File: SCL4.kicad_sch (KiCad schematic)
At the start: 4 parts

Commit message: ERC passes
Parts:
- added J1: Siemens_A1010-A263, symbol siemens_a1010-a263:Siemens_A1010-A263
- added J2: Conn_01x08, symbol Connector_Generic:Conn_01x08
- added J3: 5V out, symbol Connector:Screw_Terminal_01x02
- added J4: spare1, symbol Connector:Conn_01x01_Male
- added J5: SP1, symbol Connector:Conn_01x02_Male
- added J6: spare2, symbol Connector:Conn_01x01_Male
- added J7: SP2, symbol Connector:Conn_01x02_Male
- added JP1: LSA, symbol Jumper:Jumper_3_Open
- added JP2: LSB, symbol Jumper:Jumper_3_Open
- added JP3: LOCAL, symbol Jumper:Jumper_3_Open
- added JP4: NEXT, symbol Jumper:Jumper_3_Open
- added JP5: SYSTEM, symbol Jumper:Jumper_3_Open
- added R1, R2, R3, R4, R5, R6: 51R, symbol Device:R
- added R7, R8: 10K, symbol Device:R
- added U1: MC10H125 (20PLCC), symbol Interface:MC10H125 (20PLCC)
- added U2: MC10H124 (20PLCC), symbol Interface:MC10H124 (20PLCC)
- added U3: TRAM Size 2, symbol Transputer:TRAM Size 2
- added U5, U6: MC3487DX, Package_SO:SOIC-16_3.9x9.9mm_P1.27mm, symbol Interface_LineDriver:MC3487DX
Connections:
- net +48V: now also J1.P2 (48V+)
- net +5V: now also J3.2 (Pin_2), JP1.3 (B), JP2.3 (B), JP3.3 (B), JP4.3 (B), JP5.3 (B), U1.12 (Vcc), U2.12 (Vcc), U2.8 (CS), U3.19 (Vcc), U3.3 (Vcc), U5.12 (ENABLE), U5.12 (ENABLE), U5.16 (VCC), U5.16 (VCC), U5.16 (VCC), U5.16 (VCC), U5.4 (ENABLE), U5.4 (ENABLE), U6.12 (ENABLE), U6.12 (ENABLE), U6.16 (VCC), U6.16 (VCC), U6.16 (VCC), U6.16 (VCC), U6.4 (ENABLE), U6.4 (ENABLE)
- net -48V: now also J1.P3 (48V-)
- net -5V: now also U1.10 (Vee), U2.10 (Vee)
- net GND: now also J1.A54 (GND), J1.B1 (GND), J1.B2 (GND), J1.B3 (GND), J1.B6 (GND), J1.P1 (Gnd), J1.P4 (Stat_Gnd), J1.P5 (Gnd), J1.P6 (Gnd), J2.6 (Pin_6), J3.1 (Pin_1), JP1.1 (A), JP2.1 (A), JP3.1 (A), JP4.1 (A), JP5.1 (A), R3.2, R4.2, R5.2, R6.2, U1.20 (GND), U2.20 (GND), U3.14 (GND), U3.30 (GND), U5.8 (GND), U5.8 (GND), U5.8 (GND), U5.8 (GND), U6.8 (GND), U6.8 (GND), U6.8 (GND), U6.8 (GND)
- new net: JP1.2 (C), U3.6 (SpeedA)
- new net: JP4.2 (C), U5.9 (INPUT)
- new net: JP3.2 (C), U5.1 (INPUT)
- new net: JP2.2 (C), U3.7 (SpeedB)
- new net: J7.1 (Pin_1), U5.13 (OUT-)
- new net: J7.2 (Pin_2), U5.14 (OUT+)
- new net: R7.2, R8.2
- new net: JP5.2 (C), U6.15 (INPUT)
- new net: J6.1 (Pin_1), U5.15 (INPUT)
- new net: J5.1 (Pin_1), U5.5 (OUT-)
- new net: J5.2 (Pin_2), U5.6 (OUT+)
- new net: J4.1 (Pin_1), U5.7 (INPUT)
- new net ANALYSE: J1.A22 (/H2ANALYSE), J1.B22 (H1ANALYSE), U6.6 (OUT+)
- new net BYTE: J1.A25 (H2BYTE), J1.B25 (H1BYTE), U6.10 (OUT+)
- new net L2IN: J1.A1 (L2IN), R1.1, U1.14 (Cin)
- new net L2OUT: J1.A4 (L2OUT), R6.1, U2.19 (Cout)
- new net L3IN: J1.A7 (L3IN), R2.1, U1.19 (Din)
- new net L3OUT: J1.A10 (L3OUT), R4.1, U2.18 (Dout)
- new net LOCAL: J1.A27 (H2LOCAL), J1.B27 (H1LOCAL), U5.2 (OUT+)
- new net NEXT: J1.A31 (H2NEXT), J1.B31 (H1NEXT), U5.10 (OUT+)
- new net RESET: J1.A20 (/H2RESET), J1.B20 (H1RESET), U6.2 (OUT+)
- new net SYSTEM: J1.A23 (H2SYSTEM), J1.B23 (H1SYSYSTEM), U6.14 (OUT+)
- new net TAnalyse: J2.5 (Pin_5), U3.25 (Analyse), U6.7 (INPUT)
- new net TByte: J2.8 (Pin_8), U6.9 (INPUT)
- new net TClk: J2.1 (Pin_1), U3.8 (ClockIn)
- new net TL0In: J2.2 (Pin_2), U3.29 (L0in)
- new net TL0Out: J2.3 (Pin_3), U3.28 (L0out)
- new net TL2in: R8.1, U1.15 (Cout), U3.2 (L2in)
- new net TL2out: U2.13 (Cin), U3.1 (L2out)
- new net TL3in: R7.1, U1.17 (Dout), U3.32 (L3in)
- new net TL3out: U2.14 (Din), U3.31 (L3out)
- new net TNotError: J2.7 (Pin_7), U3.27 (/Error)
- new net TReset: J2.4 (Pin_4), U3.26 (Reset), U6.1 (INPUT)
- new net /ANALYSE: J1.A21 (H2ANALYSE), J1.B21 (/H1ANALYSE), U6.5 (OUT-)
- new net /BYTE: J1.A26 (/H2BYTE), J1.B26 (/H1BYTE), U6.11 (OUT-)
- new net /L2IN: J1.A2 (/L2IN), R1.2, U1.13 (/Cin)
- new net /L2OUT: J1.A5 (/L2OUT), R5.1, U2.15 (/Cout)
- new net /L3IN: J1.A8 (/L3IN), R2.2, U1.18 (/Din)
- new net /L3OUT: J1.A11 (/L3OUT), R3.1, U2.17 (/Dout)
- new net /LOCAL: J1.A28 (/H2LOCAL), J1.B28 (/H1LOCAL), U5.3 (OUT-)
- new net /NEXT: J1.A32 (/H2NEXT), J1.B32 (/H1NEXT), U5.11 (OUT-)
- new net /RESET: J1.A19 (H2RESET), J1.B19 (/H1RESET), U6.3 (OUT-)
- new net /SYSTEM: J1.A24 (/H2SYSTEM), J1.B24 (/H1SYSYSTEM), U6.13 (OUT-)
- no-connect marks 5 -> 239
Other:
- moved on the sheet: C1, C2, PS1, PS2

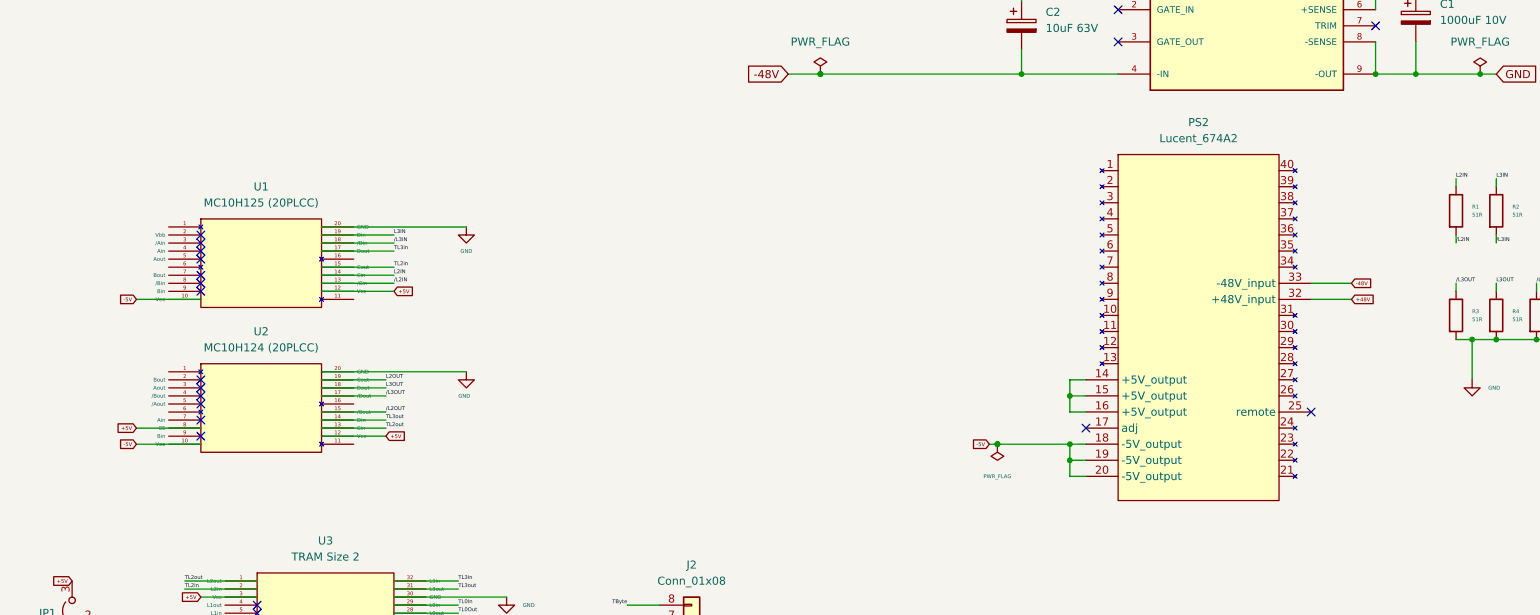
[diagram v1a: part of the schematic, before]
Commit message: swap abcd on siedecon
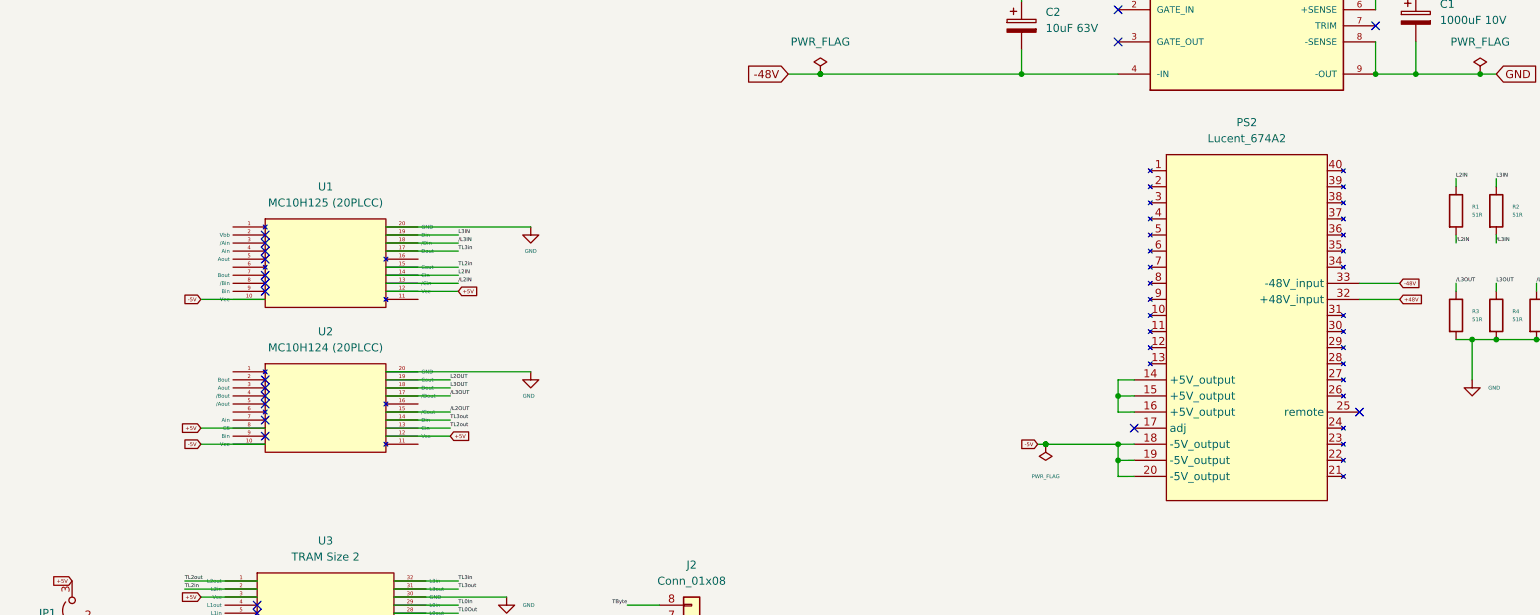
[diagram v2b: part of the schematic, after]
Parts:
- J2: footprint (none) -> Connector_PinHeader_2.54mm:PinHeader_1x08_P2.54mm_Vertical
- J3: footprint (none) -> TerminalBlock:TerminalBlock_bornier-2_P5.08mm
- J4, J6: footprint (none) -> Connector_PinHeader_2.54mm:PinHeader_1x01_P2.54mm_Vertical
- J5, J7: footprint (none) -> Connector_PinHeader_2.54mm:PinHeader_1x02_P2.54mm_Vertical
- JP1, JP2, JP3, JP4, JP5: footprint (none) -> Connector_PinHeader_2.54mm:PinHeader_1x03_P2.54mm_Vertical
- PS1: footprint CONV_VI-230-CX -> Module:vicor vi230cx
- R1, R2, R3, R4, R5, R6, R7, R8: footprint (none) -> Resistor_SMD:R_2816_7142Metric_Pad3.20x4.45mm_HandSolder
- U1, U2: footprint (none) -> Package_LCC:PLCC-20
- U3: footprint (none) -> Transputer:TRAM size 2
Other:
- moved on the sheet: PS2, U1, U2

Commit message: fp assignment
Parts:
- added C2: 100uF 63V, Capacitor_THT:CP_Radial_D10.0mm_P5.00mm, symbol Device:C_Polarized
- added D1, D2: SMCX70A, Diode_SMD:D_SMC_Handsoldering, symbol Device:D_Schottky
- added F1: 5A, Fuse:BUSSMAN SFT-1, symbol Device:Fuse
- added F2: 3A, Fuse:BUSSMAN SFT-1, symbol Device:Fuse
- added L1: INDUCTOR, Inductor_THT:L_Axial_L12.8mm_D5.8mm_P20.32mm_Horizontal_Fastron_HBCC, symbol pspice:INDUCTOR
- added R1: 10R 2%, Resistor_THT:R_Axial_DIN0207_L6.3mm_D2.5mm_P15.24mm_Horizontal, symbol Device:R
- added R2: 27R, Resistor_SMD:R_1206_3216Metric_Pad1.30x1.75mm_HandSolder, symbol Device:R
- C1: renamed from C2; footprint Capacitor_THT:CP_Axial_L29.0mm_D20.0mm_P35.00mm_Horizontal -> Capacitor_THT:CP_Radial_D5.0mm_P2.50mm
- J3: renamed from J1; footprint (none) -> SIEDECON:Siedecon 256+6
- renumbered C1 to C3, J4 to J1, J6 to J2, J5 to J4, J7 to J5, J2 to J6, J3 to J7, JP4 to JP1, JP3 to JP2, JP5 to JP3, JP1 to JP4, JP2 to JP5, R8 to R10, R1 to R3, R3 to R4, R2 to R5, R4 to R6, R5 to R7, R6 to R8, R7 to R9, U5 to U1, U6 to U2, U1 to U4, U2 to U5
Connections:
- net +48V: now also F1.2, F2.1; no longer C1.1, PS1.1 (+IN), PS2.32 (+48V_input)
- net -48V: now also D1.2 (A), D2.2 (A), L1.1; no longer PS2.33 (-48V_input)
- net -5V: now also R2.1; no longer PS2.18 (-5V_output), PS2.19 (-5V_output), PS2.20 (-5V_output)
- net GND: now also PS2.14 (+5V_output), PS2.15 (+5V_output), PS2.16 (+5V_output), R2.2
- new net: C1.1, D2.1 (K), F2.2, PS1.1 (+IN)
- new net: L1.2, R1.1
- new net: PS2.18 (-5V_output), PS2.19 (-5V_output), PS2.20 (-5V_output)
- new net +L48V: C2.2, PS2.32 (+48V_input), R1.2
- new net -L48V: C2.1, D1.1 (K), F1.1, PS2.33 (-48V_input)
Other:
- moved on the sheet: R10, R3, R4, R5, R6, R7, R8, R9

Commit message: starting routing
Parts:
- C3: footprint Capacitor_THT:CP_Axial_L26.5mm_D20.0mm_P33.00mm_Horizontal -> Capacitor_THT:CP_Radial_D13.0mm_P5.00mm
- F1, F2: footprint Fuse:BUSSMAN SFT-1 -> BUSSMAN:BUSSMAN SFT-1
- PS1: footprint Module:vicor vi230cx -> CONV_VI-230-CX
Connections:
- net +48V: now also F2.2; no longer F2.1
- net +L48V: now also C2.1, D1.1 (K), F1.1; no longer C2.2, R1.2
- net -5V: no longer R2.1
- net -L48V: now also C2.2, R1.2; no longer C2.1, D1.1 (K), F1.1
- net at C1.1, D2.1 (K), PS1.1 (+IN): now also F2.1; no longer F2.2
- net at PS2.17 (adj): now also R2.1
- no-connect marks 239 -> 238
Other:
- moved on the sheet: PS2

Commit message: board layout complete
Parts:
- PS1: footprint CONV_VI-230-CX -> Module:vicor vi230cx
- R10, R3, R4, R5, R6, R7, R8, R9: footprint Resistor_SMD:R_2816_7142Metric_Pad3.20x4.45mm_HandSolder -> Resistor_SMD:R_1206_3216Metric_Pad1.30x1.75mm_HandSolder
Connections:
- net -5V: now also PS2.18 (-5V_output), PS2.19 (-5V_output), PS2.20 (-5V_output), R4.2, R6.2, R7.2, R8.2
- net GND: now also R10.2, R9.2; no longer R4.2, R6.2, R7.2, R8.2
- net SpeedA: now reaches JP4.2 (C), U3.6 (SpeedA)
- net SpeedB: now reaches JP5.2 (C), U3.7 (SpeedB)
- net +L48V: no longer names the net of C2.1, D1.1 (K), F1.1, PS2.32 (+48V_input)
- net -L48V: no longer names the net of C2.2, PS2.33 (-48V_input), R1.2
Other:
- moved on the sheet: R2

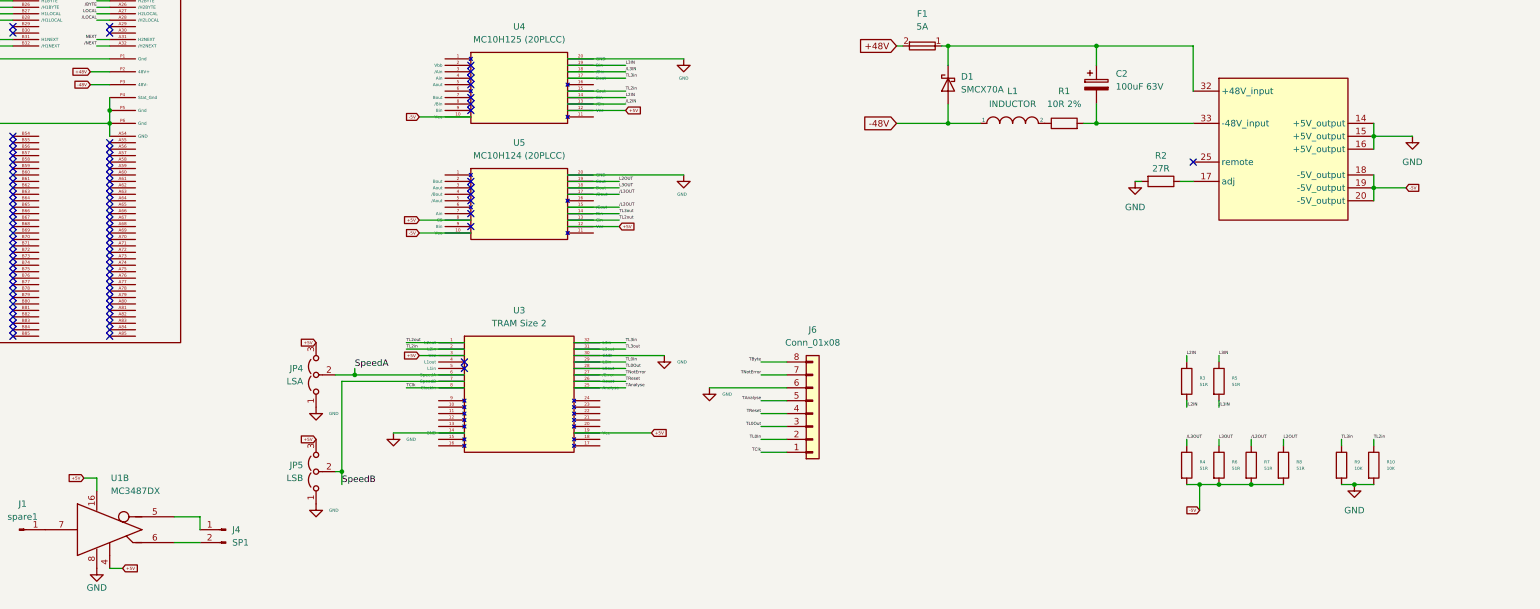
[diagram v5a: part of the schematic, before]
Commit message: fix static gnd pin
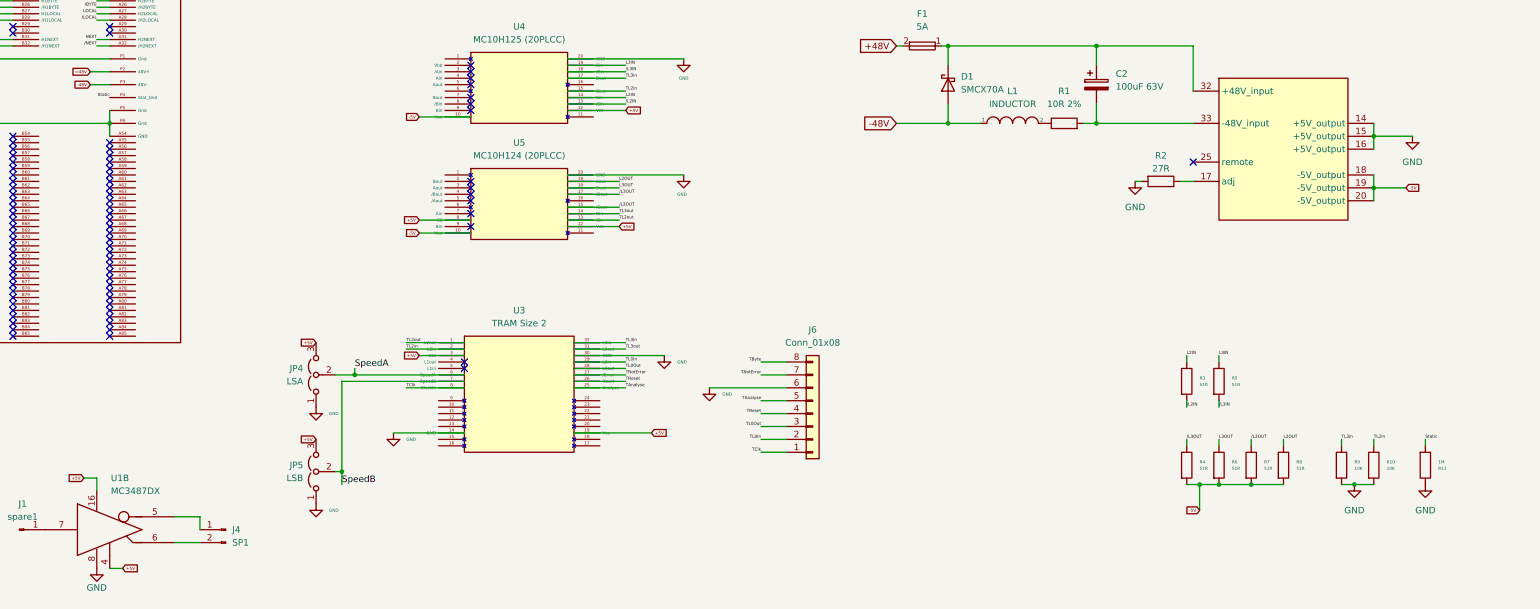
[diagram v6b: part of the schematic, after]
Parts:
- added R11: 1M, Resistor_SMD:R_1206_3216Metric_Pad1.30x1.75mm_HandSolder, symbol Device:R
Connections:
- net GND: now also R11.1; no longer J3.P4 (Stat_Gnd)
- new net Static: J3.P4 (Stat_Gnd), R11.2
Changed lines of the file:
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@@
   (junction (at 142.24 132.08) (diameter 0) (color 0 0 0 0)
   )
-  (junction (at 93.98 80.01) (diameter 0) (color 0 0 0 0)
-  )
   (junction (at 346.71 45.72) (diameter 0) (color 0 0 0 0)
   )
@@
     (stroke (width 0) (type default) (color 0 0 0 0))
   )
-  (wire (pts (xy 93.98 77.47) (xy 93.98 80.01))
-    (stroke (width 0) (type default) (color 0 0 0 0))
-  )
   (wire (pts (xy 342.9 82.55) (xy 342.9 85.09))
     (stroke (width 0) (type default) (color 0 0 0 0))
@@
     (stroke (width 0) (type default) (color 0 0 0 0))
   )
+  (wire (pts (xy 353.06 144.78) (xy 353.06 146.05))
+    (stroke (width 0) (type default) (color 0 0 0 0))
+  )
   (wire (pts (xy 222.25 129.54) (xy 227.33 129.54))
     (stroke (width 0) (type default) (color 0 0 0 0))
@@
     (effects (font (size 1.27 1.27)) (justify left bottom))
   )
+  (label "Static" (at 93.98 77.47 180)
+    (effects (font (size 0.6 0.6)) (justify right bottom))
+  )
   (label "L3IN" (at 195.58 71.12 0)
     (effects (font (size 0.6 0.6)) (justify left bottom))
@@
     (effects (font (size 0.6 0.6)) (justify left bottom))
   )
+  (label "Static" (at 353.06 144.78 0)
+    (effects (font (size 0.6 0.6)) (justify left bottom))
+  )
   (label "TL3out" (at 195.58 127 0)
     (effects (font (size 0.6 0.6)) (justify left bottom))
@@
     (pin "8")
   )
+  (symbol (lib_id "Device:R") (at 353.06 149.86 0) (mirror x) (unit 1)
+    (in_bom yes) (on_board yes)
+    (property "Reference" "R11" (id 0) (at 355.6 150.495 0)
+      (effects (font (size 0.6 0.6)) (justify left))
+    )
+    (property "Value" "1M" (id 1) (at 355.6 149.225 0)
+      (effects (font (size 0.6 0.6)) (justify left))
+    )
+    (property "Footprint" "Resistor_SMD:R_1206_3216Metric_Pad1.30x1.75mm_HandSolder" (id 2) (at 351.282 149.86 90)
+      (effects (font (size 1.27 1.27)) hide)
+    )
+    (property "Datasheet" "~" (id 3) (at 353.06 149.86 0)
+      (effects (font (size 1.27 1.27)) hide)
+    )
+    (pin "1")
+    (pin "2")
+  )
   (symbol (lib_id "Jumper:Jumper_3_Open") (at 25.4 154.94 0) (unit 1)
     (in_bom yes) (on_board yes) (fields_autoplaced)
@@
     (pin "1")
   )
+  (symbol (lib_id "power:GND") (at 353.06 153.67 0) (unit 1)
+    (in_bom yes) (on_board yes) (fields_autoplaced)
+    (property "Reference" "#PWR0103" (id 0) (at 353.06 160.02 0)
+      (effects (font (size 1.27 1.27)) hide)
+    )
+    (property "Value" "GND" (id 1) (at 353.06 158.75 0))
+    (property "Footprint" "" (id 2) (at 353.06 153.67 0)
+      (effects (font (size 1.27 1.27)) hide)
+    )
+    (property "Datasheet" "" (id 3) (at 353.06 153.67 0)
+      (effects (font (size 1.27 1.27)) hide)
+    )
+    (pin "1")
+  )
   (symbol (lib_id "power:GND") (at 39.37 231.14 0) (unit 1)
     (in_bom yes) (on_board yes) (fields_autoplaced)
@@
       (reference "#PWR0102") (unit 1) (value "GND") (footprint "")
     )
+    (path "/ad426314-23f3-4eac-a899-4f215807e7bc"
+      (reference "#PWR0103") (unit 1) (value "GND") (footprint "")
+    )
     (path "/9596e356-a06d-4e23-8960-152ed06df59f"
       (reference "C1") (unit 1) (value "10uF 63V ") (footprint "Capacitor_THT:CP_Radial_D5.0mm_P2.50mm")
@@
       (reference "R10") (unit 1) (value "10K") (footprint "Resistor_SMD:R_1206_3216Metric_Pad1.30x1.75mm_HandSolder")
     )
+    (path "/80285976-68fa-4207-aee5-0a15c484c5db"
+      (reference "R11") (unit 1) (value "1M") (footprint "Resistor_SMD:R_1206_3216Metric_Pad1.30x1.75mm_HandSolder")
+    )
     (path "/0916478b-b511-473d-a1e4-457c84bf39e9"
